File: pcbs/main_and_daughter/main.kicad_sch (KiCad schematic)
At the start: 4 parts

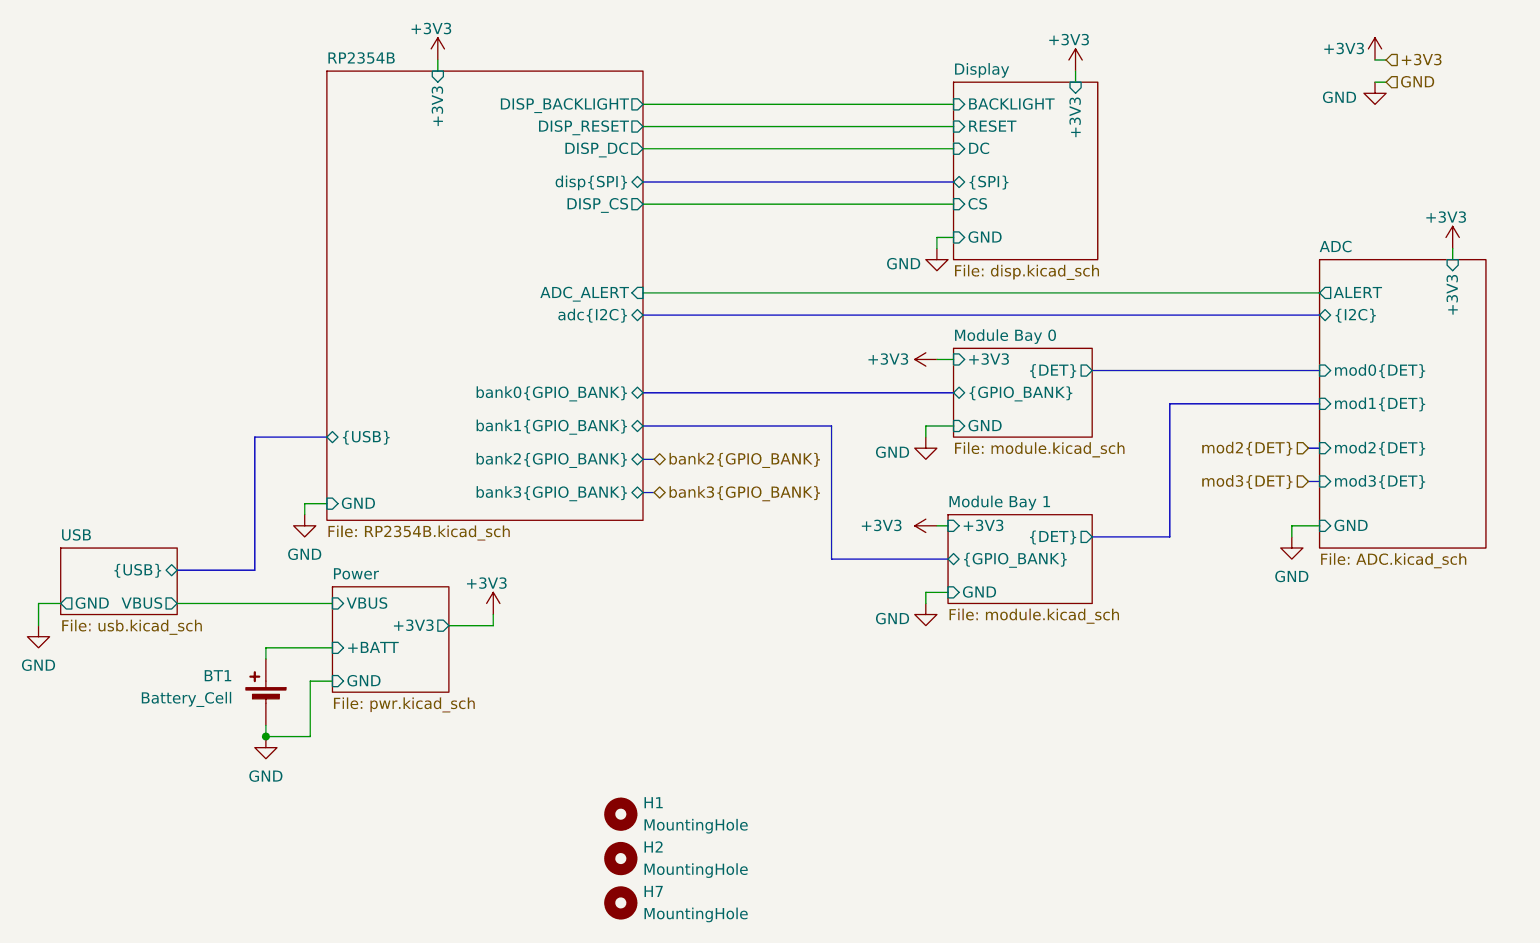
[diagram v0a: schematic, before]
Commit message: removed display brightness control, ran out of pin
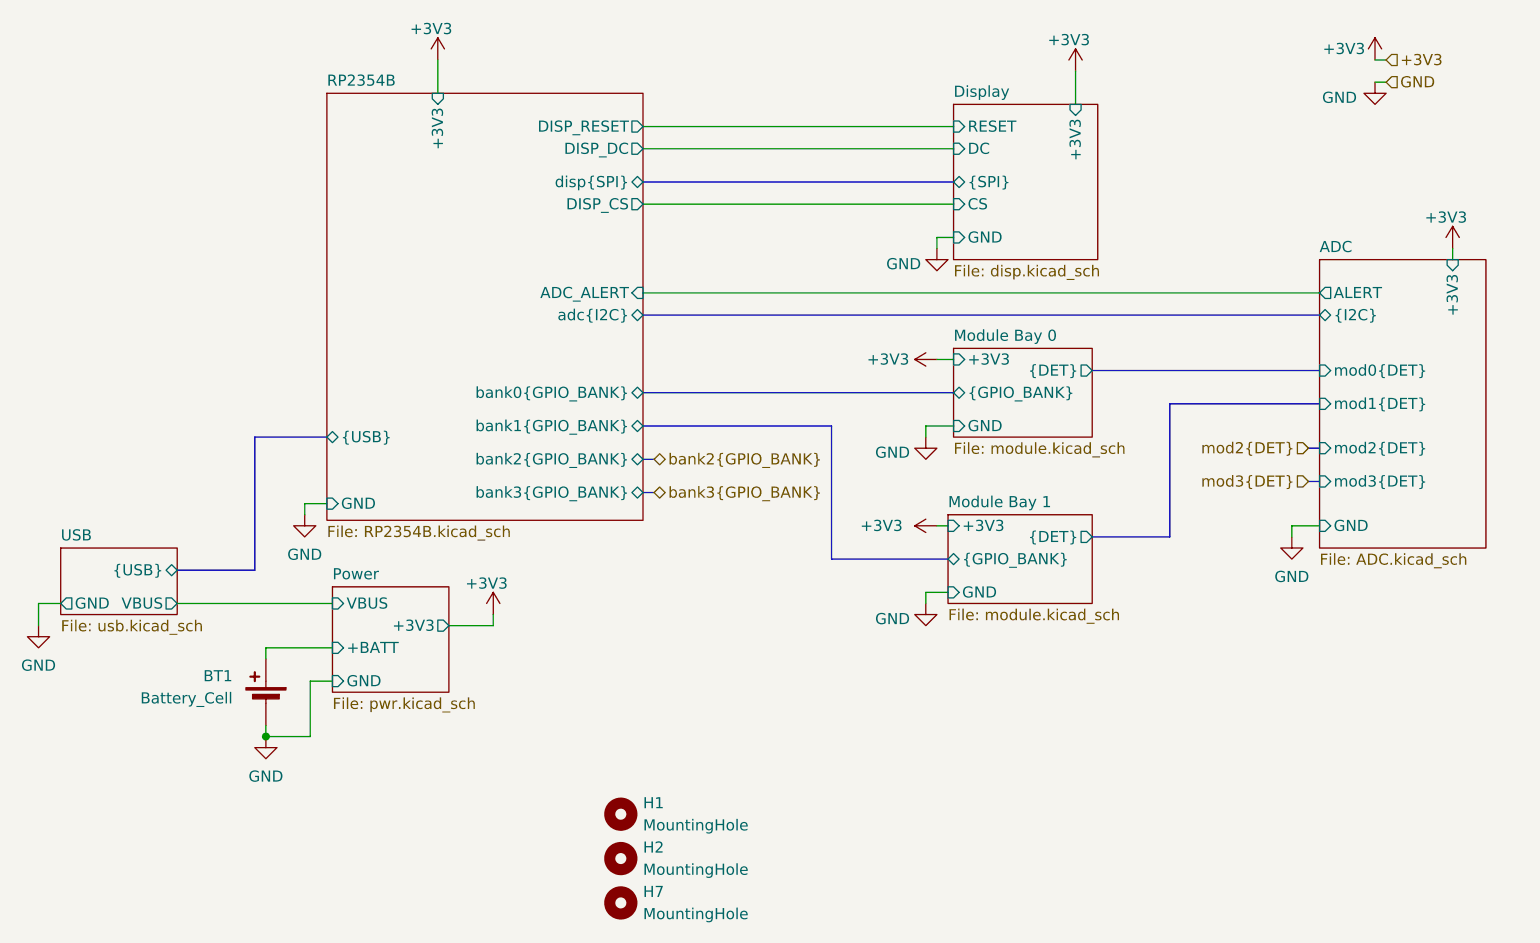
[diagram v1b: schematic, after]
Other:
- sheet Display ports: added none; removed BACKLIGHT
- sheet RP2354B ports: added none; removed DISP_BACKLIGHT
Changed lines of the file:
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@@
 	(wire
 		(pts
-			(xy 122.555 49.53) (xy 122.555 50.8)
+			(xy 122.555 49.53) (xy 122.555 53.34)
 		)
 		(stroke
@@
 	(wire
 		(pts
-			(xy 146.05 54.61) (xy 181.61 54.61)
-		)
-		(stroke
-			(width 0)
-			(type default)
-		)
-	)
-	(wire
-		(pts
 			(xy 238.76 71.12) (xy 238.76 72.39)
 		)
@@
 	(wire
 		(pts
-			(xy 195.58 50.8) (xy 195.58 52.07)
+			(xy 195.58 50.8) (xy 195.58 54.61)
 		)
 		(stroke
@@
 	)
 	(sheet
-		(at 181.61 52.07)
-		(size 16.51 20.32)
+		(at 181.61 54.61)
+		(size 16.51 17.78)
 		(exclude_from_sim no)
 		(in_bom yes)
@@
 		)
 		(property "Sheetname" "Display"
-			(at 181.61 51.3584 0)
+			(at 181.61 53.8984 0)
 			(show_name no)
 			(do_not_autoplace no)
@@
 			)
 		)
-		(pin "BACKLIGHT" input
-			(at 181.61 54.61 180)
-			(effects
-				(font
-					(size 1.27 1.27)
-				)
-				(justify left)
-			)
-		)
 		(pin "CS" input
 			(at 181.61 66.04 180)
@@
 		)
 		(pin "+3V3" input
-			(at 195.58 52.07 90)
+			(at 195.58 54.61 90)
 			(effects
 				(font
@@
 	)
 	(sheet
-		(at 109.855 50.8)
-		(size 36.195 51.435)
+		(at 109.855 53.34)
+		(size 36.195 48.895)
 		(exclude_from_sim no)
 		(in_bom yes)
@@
 		)
 		(property "Sheetname" "RP2354B"
-			(at 109.855 50.0884 0)
+			(at 109.855 52.6284 0)
 			(show_name no)
 			(do_not_autoplace no)
@@
 			)
 		)
-		(pin "DISP_BACKLIGHT" output
-			(at 146.05 54.61 0)
-			(effects
-				(font
-					(size 1.27 1.27)
-				)
-				(justify right)
-			)
-		)
 		(pin "DISP_CS" output
 			(at 146.05 66.04 0)
@@
 		)
 		(pin "+3V3" input
-			(at 122.555 50.8 90)
-			(effects
-				(font
+			(at 122.555 53.34 90)
+			(effects
+				(font

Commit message: added titles to schematic
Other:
- title: (none) -> Main Board
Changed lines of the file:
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@@
 	(generator_version "10.0")
 	(paper "A4")
+	(title_block
+		(title "Main Board")
+	)
 	(junction
 		(at 102.87 127)

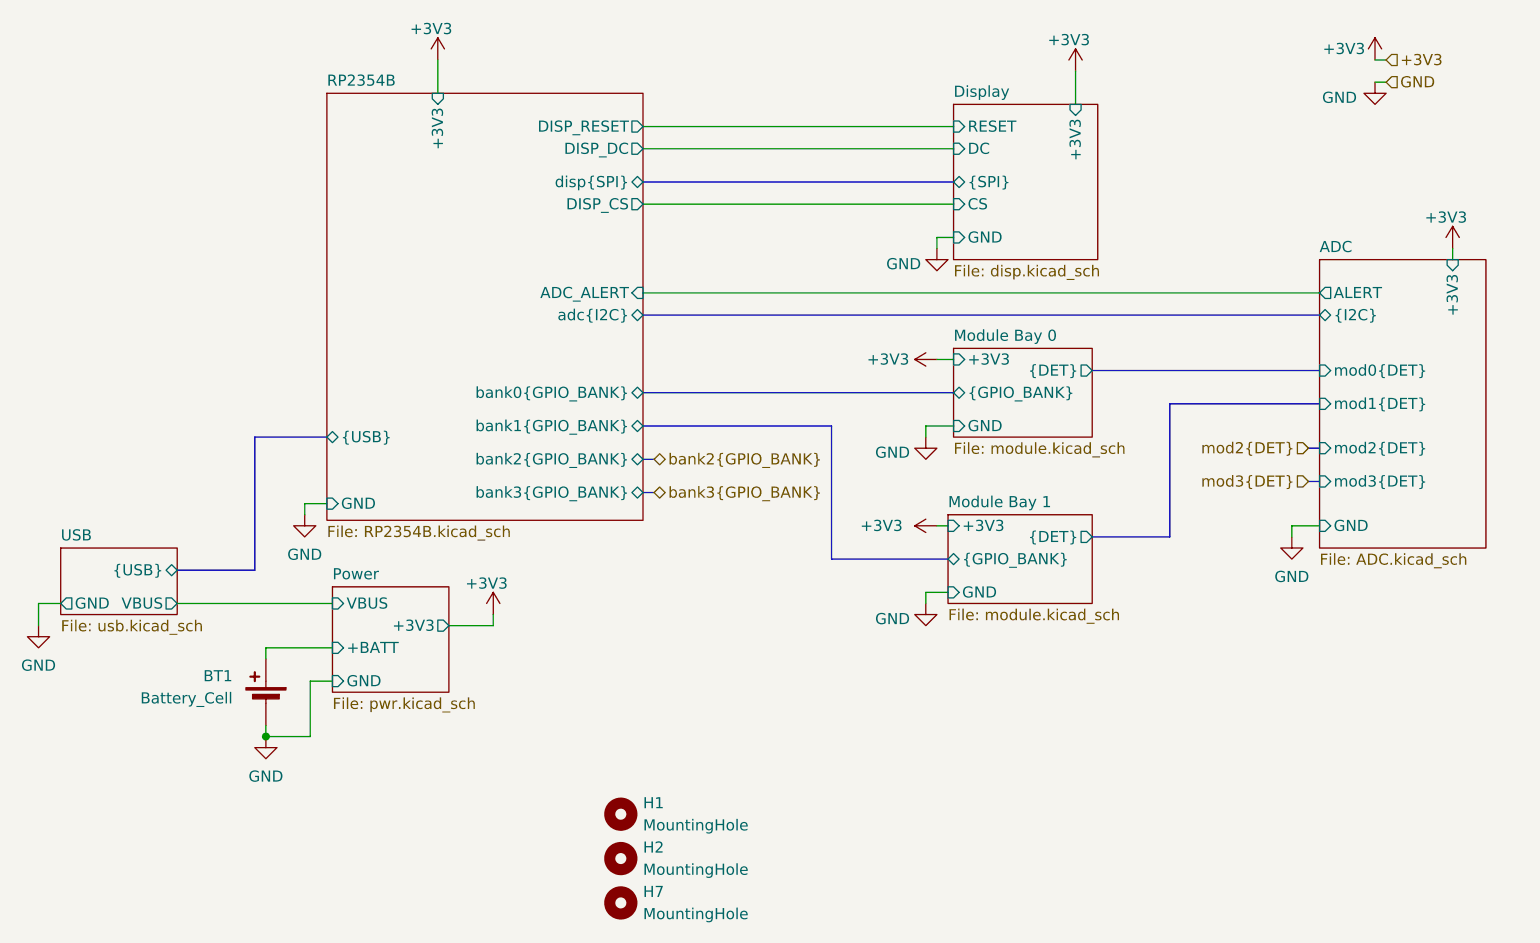
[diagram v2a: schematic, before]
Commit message: added back display brightness, removed adc allert on pcb
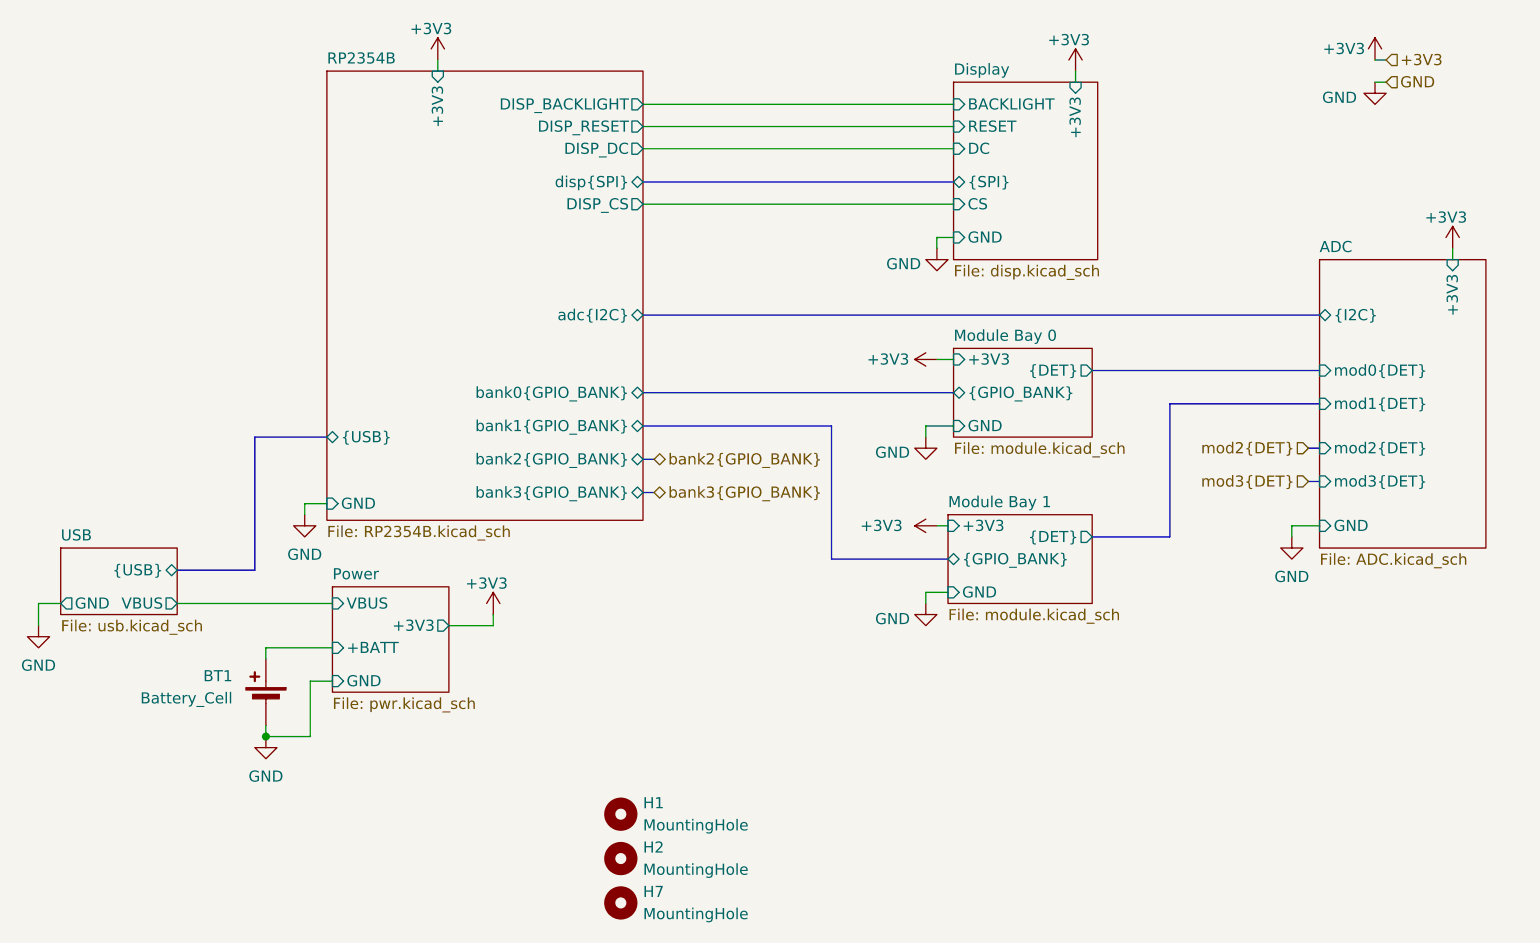
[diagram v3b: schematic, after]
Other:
- sheet ADC ports: added none; removed ALERT
- sheet Display ports: added BACKLIGHT; removed none
- sheet RP2354B ports: added DISP_BACKLIGHT; removed ADC_ALERT
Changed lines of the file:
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@@
 	(wire
 		(pts
-			(xy 122.555 49.53) (xy 122.555 53.34)
+			(xy 122.555 49.53) (xy 122.555 50.8)
 		)
 		(stroke
@@
 	(wire
 		(pts
-			(xy 146.05 76.2) (xy 223.52 76.2)
-		)
-		(stroke
-			(width 0)
-			(type default)
-		)
-	)
-	(wire
-		(pts
 			(xy 220.345 104.14) (xy 220.345 102.87)
 		)
@@
 	(wire
 		(pts
+			(xy 146.05 54.61) (xy 181.61 54.61)
+		)
+		(stroke
+			(width 0)
+			(type default)
+		)
+	)
+	(wire
+		(pts
 			(xy 238.76 71.12) (xy 238.76 72.39)
 		)
@@
 	(wire
 		(pts
-			(xy 195.58 50.8) (xy 195.58 54.61)
+			(xy 195.58 50.8) (xy 195.58 52.07)
 		)
 		(stroke
@@
 	)
 	(sheet
-		(at 181.61 54.61)
-		(size 16.51 17.78)
+		(at 181.61 52.07)
+		(size 16.51 20.32)
 		(exclude_from_sim no)
 		(in_bom yes)
@@
 		)
 		(property "Sheetname" "Display"
-			(at 181.61 53.8984 0)
+			(at 181.61 51.3584 0)
 			(show_name no)
 			(do_not_autoplace no)
@@
 			)
 		)
+		(pin "BACKLIGHT" input
+			(at 181.61 54.61 180)
+			(effects
+				(font
+					(size 1.27 1.27)
+				)
+				(justify left)
+			)
+		)
 		(pin "CS" input
 			(at 181.61 66.04 180)
@@
 		)
 		(pin "+3V3" input
-			(at 195.58 54.61 90)
+			(at 195.58 52.07 90)
 			(effects
 				(font
@@
 			)
 		)
-		(pin "ALERT" output
-			(at 223.52 76.2 180)
-			(effects
-				(font
-					(size 1.27 1.27)
-				)
-				(justify left)
-			)
-		)
 		(pin "mod0{DET}" input
 			(at 223.52 85.09 180)
@@
 	)
 	(sheet
-		(at 109.855 53.34)
-		(size 36.195 48.895)
+		(at 109.855 50.8)
+		(size 36.195 51.435)
 		(exclude_from_sim no)
 		(in_bom yes)
@@
 		)
 		(property "Sheetname" "RP2354B"
-			(at 109.855 52.6284 0)
+			(at 109.855 50.0884 0)
 			(show_name no)
 			(do_not_autoplace no)
@@
 			)
 		)
-		(pin "ADC_ALERT" input
-			(at 146.05 76.2 0)
-			(effects
-				(font
-					(size 1.27 1.27)
-				)
-				(justify right)
-			)
-		)
 		(pin "adc{I2C}" bidirectional
 			(at 146.05 78.74 0)
@@
 			)
 		)
+		(pin "DISP_BACKLIGHT" output
+			(at 146.05 54.61 0)
+			(effects
+				(font
+					(size 1.27 1.27)
+				)
+				(justify right)
+			)
+		)
 		(pin "DISP_CS" output
 			(at 146.05 66.04 0)
@@
 		)
 		(pin "+3V3" input
-			(at 122.555 53.34 90)
-			(effects
-				(font
+			(at 122.555 50.8 90)
+			(effects
+				(font
